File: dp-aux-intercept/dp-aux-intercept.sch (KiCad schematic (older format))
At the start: 24 parts, among them J1 CONN_02X03, J2 CONN_02X03

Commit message: Initial scatter.
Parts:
- CCAN1, CCAP1, CDAN1, CDAP1: footprint (none) -> Capacitors_SMD:C_0805_HandSoldering
- DPC1, DPD1: footprint (none) -> display_port:display_port
- J1, J2: footprint (none) -> Pin_Headers:Pin_Header_Straight_2x03
- PAUX1, PCONF1: footprint (none) -> Pin_Headers:Pin_Header_Straight_2x06
- RCAN1, RCAN2, RCAP1, RCAP2, RCCFG1, RCCFG2, RCHPD1, RDAN1, RDAN2, RDAP1, RDAP2, RDCFG1, RDCFG2, RDHPD1: footprint (none) -> Resistors_SMD:R_0603_HandSoldering
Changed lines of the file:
@@
 F 0 "DPC1" H 1510 3310 60  0000 C CNN
 F 1 "DISPLAY_PORT" V 2260 2210 60  0000 C CNN
-F 2 "" H 2060 2210 60  0000 C CNN
+F 2 "display_port:display_port" H 2060 2210 60  0001 C CNN
 F 3 "" H 2060 2210 60  0000 C CNN
 	1    2110 2210
@@
 F 0 "PAUX1" H 5510 4690 50  0000 C CNN
 F 1 "CONN_02X06" H 5510 3990 50  0000 C CNN
-F 2 "" H 5510 3140 60  0000 C CNN
+F 2 "Pin_Headers:Pin_Header_Straight_2x06" H 5510 3140 60  0001 C CNN
 F 3 "" H 5510 3140 60  0000 C CNN
 	1    5510 4340
@@
 F 0 "DPD1" H 8400 3310 60  0000 C CNN
 F 1 "DISPLAY_PORT" V 9150 2210 60  0000 C CNN
-F 2 "" H 8950 2210 60  0000 C CNN
+F 2 "display_port:display_port" H 8950 2210 60  0001 C CNN
 F 3 "" H 8950 2210 60  0000 C CNN
 	1    9000 2210
@@
 F 0 "PCONF1" H 5580 3110 50  0000 C CNN
 F 1 "CONN_02X06" H 5580 2410 50  0000 C CNN
-F 2 "" H 5580 1560 60  0000 C CNN
+F 2 "Pin_Headers:Pin_Header_Straight_2x06" H 5580 1560 60  0001 C CNN
 F 3 "" H 5580 1560 60  0000 C CNN
 	1    5580 2760
@@
 F 0 "RDCFG1" V 7230 2890 50  0000 C CNN
 F 1 "1M" V 7150 2890 50  0000 C CNN
-F 2 "" V 7080 2890 30  0000 C CNN
+F 2 "Resistors_SMD:R_0603_HandSoldering" V 7080 2890 30  0001 C CNN
 F 3 "" H 7150 2890 30  0000 C CNN
 	1    7150 2890
@@
 F 0 "RDCFG2" V 7230 3060 50  0000 C CNN
 F 1 "5M" V 7150 3060 50  0000 C CNN
-F 2 "" V 7080 3060 30  0000 C CNN
+F 2 "Resistors_SMD:R_0603_HandSoldering" V 7080 3060 30  0001 C CNN
 F 3 "" H 7150 3060 30  0000 C CNN
 	1    7150 3060
@@
 F 0 "RDHPD1" V 7230 3230 50  0000 C CNN
 F 1 "100K" V 7150 3230 50  0000 C CNN
-F 2 "" V 7080 3230 30  0000 C CNN
+F 2 "Resistors_SMD:R_0603_HandSoldering" V 7080 3230 30  0001 C CNN
 F 3 "" H 7150 3230 30  0000 C CNN
 	1    7150 3230
@@
 F 0 "J2" H 6590 3190 50  0000 C CNN
 F 1 "CONN_02X03" H 6590 2790 50  0000 C CNN
-F 2 "" H 6590 1790 60  0000 C CNN
+F 2 "Pin_Headers:Pin_Header_Straight_2x03" H 6590 1790 60  0001 C CNN
 F 3 "" H 6590 1790 60  0000 C CNN
 	1    6590 2990
@@
 F 0 "RCCFG1" V 4040 2890 50  0000 C CNN
 F 1 "1M" V 3960 2890 50  0000 C CNN
-F 2 "" V 3890 2890 30  0000 C CNN
+F 2 "Resistors_SMD:R_0603_HandSoldering" V 3890 2890 30  0001 C CNN
 F 3 "" H 3960 2890 30  0000 C CNN
 	1    3960 2890
@@
 F 0 "RCCFG2" V 4040 3060 50  0000 C CNN
 F 1 "5M" V 3960 3060 50  0000 C CNN
-F 2 "" V 3890 3060 30  0000 C CNN
+F 2 "Resistors_SMD:R_0603_HandSoldering" V 3890 3060 30  0001 C CNN
 F 3 "" H 3960 3060 30  0000 C CNN
 	1    3960 3060
@@
 F 0 "RCHPD1" V 4040 3230 50  0000 C CNN
 F 1 "100K" V 3960 3230 50  0000 C CNN
-F 2 "" V 3890 3230 30  0000 C CNN
+F 2 "Resistors_SMD:R_0603_HandSoldering" V 3890 3230 30  0001 C CNN
 F 3 "" H 3960 3230 30  0000 C CNN
 	1    3960 3230
@@
 F 0 "J1" H 4520 3190 50  0000 C CNN
 F 1 "CONN_02X03" H 4520 2790 50  0000 C CNN
-F 2 "" H 4520 1790 60  0000 C CNN
+F 2 "Pin_Headers:Pin_Header_Straight_2x03" H 4520 1790 60  0001 C CNN
 F 3 "" H 4520 1790 60  0000 C CNN
 	1    4520 2990
@@
 F 0 "RCAP1" V 3990 4270 50  0000 C CNN
 F 1 "100K" V 3910 4270 50  0000 C CNN
-F 2 "" V 3840 4270 30  0000 C CNN
+F 2 "Resistors_SMD:R_0603_HandSoldering" V 3840 4270 30  0001 C CNN
 F 3 "" H 3910 4270 30  0000 C CNN
 	1    3910 4270
@@
 F 0 "RCAN1" V 3990 4640 50  0000 C CNN
 F 1 "100K" V 3910 4640 50  0000 C CNN
-F 2 "" V 3840 4640 30  0000 C CNN
+F 2 "Resistors_SMD:R_0603_HandSoldering" V 3840 4640 30  0001 C CNN
 F 3 "" H 3910 4640 30  0000 C CNN
 	1    3910 4640
@@
 F 0 "RCAP2" V 4440 4270 50  0000 C CNN
 F 1 "50" V 4360 4270 50  0000 C CNN
-F 2 "" V 4290 4270 30  0000 C CNN
+F 2 "Resistors_SMD:R_0603_HandSoldering" V 4290 4270 30  0001 C CNN
 F 3 "" H 4360 4270 30  0000 C CNN
 	1    4360 4270
@@
 F 0 "RCAN2" V 4440 4640 50  0000 C CNN
 F 1 "50" V 4360 4640 50  0000 C CNN
-F 2 "" V 4290 4640 30  0000 C CNN
+F 2 "Resistors_SMD:R_0603_HandSoldering" V 4290 4640 30  0001 C CNN
 F 3 "" H 4360 4640 30  0000 C CNN
 	1    4360 4640
@@
 F 0 "CCAP1" H 4165 4190 50  0000 L CNN
 F 1 "C" H 4165 3990 50  0000 L CNN
-F 2 "" H 4178 3940 30  0000 C CNN
+F 2 "Capacitors_SMD:C_0805_HandSoldering" H 4178 3940 30  0001 C CNN
 F 3 "" H 4140 4090 60  0000 C CNN
 	1    4140 4090
@@
 F 0 "CCAN1" H 4165 4930 50  0000 L CNN
 F 1 "C" H 4165 4730 50  0000 L CNN
-F 2 "" H 4178 4680 30  0000 C CNN
+F 2 "Capacitors_SMD:C_0805_HandSoldering" H 4178 4680 30  0001 C CNN
 F 3 "" H 4140 4830 60  0000 C CNN
 	1    4140 4830
@@
 F 0 "RDAP2" V 6790 4270 50  0000 C CNN
 F 1 "50" V 6710 4270 50  0000 C CNN
-F 2 "" V 6640 4270 30  0000 C CNN
+F 2 "Resistors_SMD:R_0603_HandSoldering" V 6640 4270 30  0001 C CNN
 F 3 "" H 6710 4270 30  0000 C CNN
 	1    6710 4270
@@
 F 0 "RDAN2" V 6790 4640 50  0000 C CNN
 F 1 "50" V 6710 4640 50  0000 C CNN
-F 2 "" V 6640 4640 30  0000 C CNN
+F 2 "Resistors_SMD:R_0603_HandSoldering" V 6640 4640 30  0001 C CNN
 F 3 "" H 6710 4640 30  0000 C CNN
 	1    6710 4640
@@
 F 0 "RDAP1" V 7240 4270 50  0000 C CNN
 F 1 "10K" V 7160 4270 50  0000 C CNN
-F 2 "" V 7090 4270 30  0000 C CNN
+F 2 "Resistors_SMD:R_0603_HandSoldering" V 7090 4270 30  0001 C CNN
 F 3 "" H 7160 4270 30  0000 C CNN
 	1    7160 4270
@@
 F 0 "RDAN1" V 7240 4640 50  0000 C CNN
 F 1 "10K" V 7160 4640 50  0000 C CNN
-F 2 "" V 7090 4640 30  0000 C CNN
+F 2 "Resistors_SMD:R_0603_HandSoldering" V 7090 4640 30  0001 C CNN
 F 3 "" H 7160 4640 30  0000 C CNN
 	1    7160 4640
@@
 F 0 "CDAP1" H 6965 4190 50  0000 L CNN
 F 1 "C" H 6965 3990 50  0000 L CNN
-F 2 "" H 6978 3940 30  0000 C CNN
+F 2 "Capacitors_SMD:C_0805_HandSoldering" H 6978 3940 30  0001 C CNN
 F 3 "" H 6940 4090 60  0000 C CNN
 	1    6940 4090
@@
 F 0 "CDAN1" H 6965 4930 50  0000 L CNN
 F 1 "C" H 6965 4730 50  0000 L CNN
-F 2 "" H 6978 4680 30  0000 C CNN
+F 2 "Capacitors_SMD:C_0805_HandSoldering" H 6978 4680 30  0001 C CNN
 F 3 "" H 6940 4830 60  0000 C CNN
 	1    6940 4830

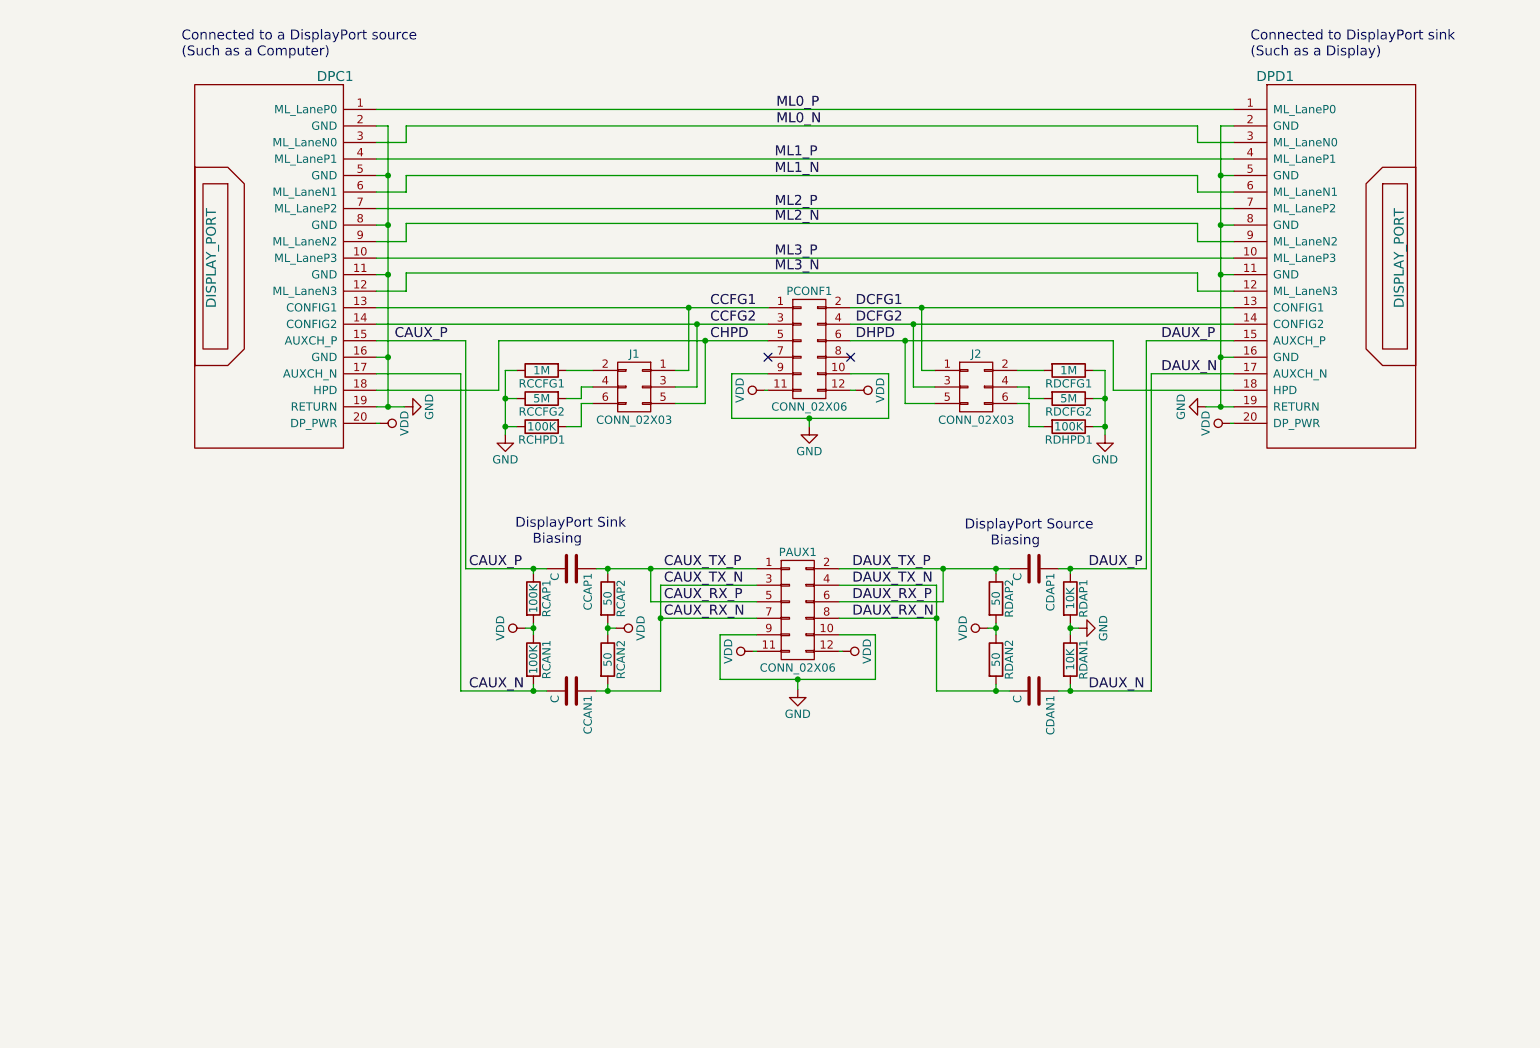
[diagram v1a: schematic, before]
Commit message: Adding schematic description.
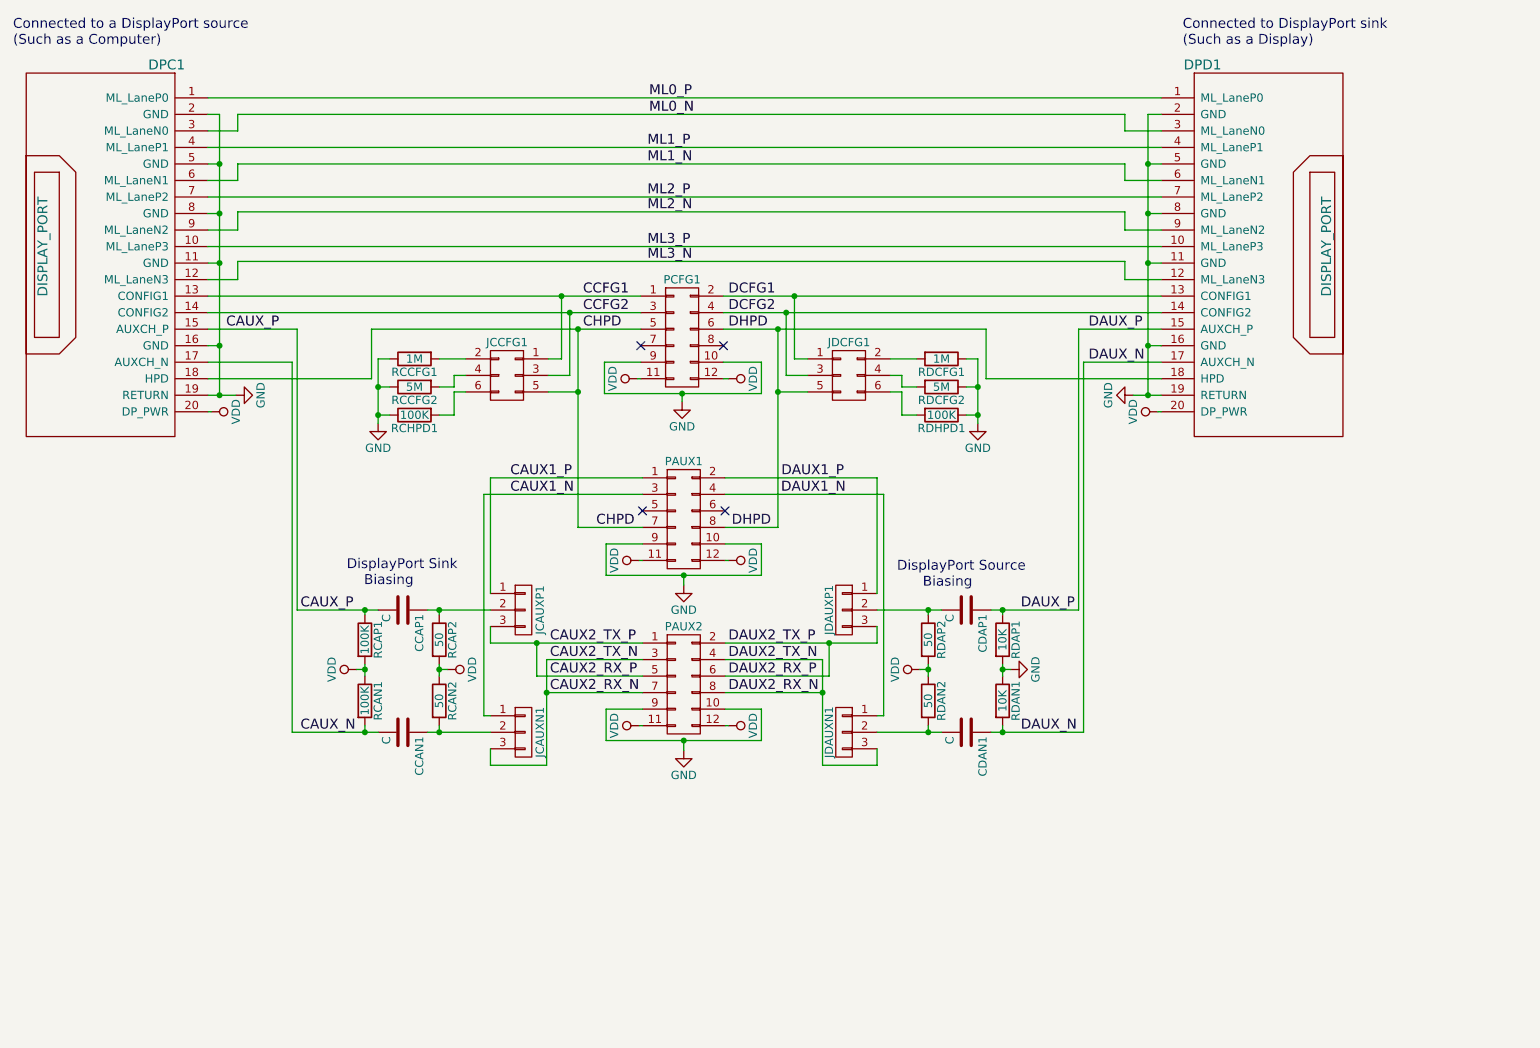
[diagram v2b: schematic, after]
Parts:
- added JCAUXN1, JCAUXP1, JDAUXN1, JDAUXP1: CONN_01X03, symbol CONN_01X03
- added PAUX1: CONN_02X06, Pin_Headers:Pin_Header_Straight_2x06, symbol CONN_02X06
- renumbered J1 to JCCFG1, J2 to JDCFG1, PAUX1 to PAUX2, PCONF1 to PCFG1
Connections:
- net CHPD: now also PAUX1.7 (P7)
- net DHPD: now also PAUX1.8 (P8)
- net GND: now also PAUX1.10 (P10), PAUX1.9 (P9)
- net VDD: now also PAUX1.11 (P11), PAUX1.12 (P12)
- net CAUX_RX_N: no longer names the net of CCAN1.1, RCAN2.2
- net CAUX_RX_N: now also JCAUXN1.2 (P2); no longer PAUX2.3 (P3), PAUX2.7 (P7)
- net CAUX_RX_P: no longer names the net of CCAP1.1, RCAP2.1
- net CAUX_RX_P: now also JCAUXP1.2 (P2); no longer PAUX2.1 (P1), PAUX2.5 (P5)
- net DAUX_RX_N: no longer names the net of CDAN1.2, RDAN2.2
- net DAUX_RX_N: now also JDAUXN1.2 (P2); no longer PAUX2.4 (P4), PAUX2.8 (P8)
- net DAUX_RX_P: no longer names the net of CDAP1.2, RDAP2.1
- net DAUX_RX_P: now also JDAUXP1.2 (P2); no longer PAUX2.2 (P2), PAUX2.6 (P6)
- new net CAUX1_N: JCAUXN1.1 (P1), PAUX1.3 (P3)
- new net CAUX1_P: JCAUXP1.1 (P1), PAUX1.1 (P1)
- new net CAUX2_RX_N: JCAUXN1.3 (P3), PAUX2.3 (P3), PAUX2.7 (P7)
- new net CAUX2_RX_P: JCAUXP1.3 (P3), PAUX2.1 (P1), PAUX2.5 (P5)
- new net DAUX1_N: JDAUXN1.1 (P1), PAUX1.4 (P4)
- new net DAUX1_P: JDAUXP1.1 (P1), PAUX1.2 (P2)
- new net DAUX2_RX_N: JDAUXN1.3 (P3), PAUX2.4 (P4), PAUX2.8 (P8)
- new net DAUX2_RX_P: JDAUXP1.3 (P3), PAUX2.2 (P2), PAUX2.6 (P6)
- no-connect marks 2 -> 4
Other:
- moved on the sheet: CCAN1, CCAP1, CDAN1, CDAP1, DPC1, DPD1, JCCFG1, JDCFG1, PAUX2, PCFG1, RCAN1, RCAN2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

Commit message: Changing to using the through-hole DisplayPort connectors.
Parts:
- DPC1, DPD1: footprint display_port:display_port -> 2040204-1:2040210-1
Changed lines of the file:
@@
 F 0 "DPC1" H 490 3240 60  0000 C CNN
 F 1 "DISPLAY_PORT" V 1240 2140 60  0000 C CNN
-F 2 "display_port:display_port" H 1040 2140 60  0001 C CNN
+F 2 "2040204-1:2040210-1" H 1040 2140 60  0001 C CNN
 F 3 "" H 1040 2140 60  0000 C CNN
 	1    1090 2140
@@
 F 0 "DPD1" H 7960 3240 60  0000 C CNN
 F 1 "DISPLAY_PORT" V 8710 2140 60  0000 C CNN
-F 2 "display_port:display_port" H 8510 2140 60  0001 C CNN
+F 2 "2040204-1:2040210-1" H 8510 2140 60  0001 C CNN
 F 3 "" H 8510 2140 60  0000 C CNN
 	1    8560 2140
@@
 	1940 1340 2010 1340
 Wire Wire Line
-	2010 1340 2010 1640
-Wire Wire Line
-	2010 1640 2010 1940
-Wire Wire Line
-	2010 1940 2010 2240
-Wire Wire Line
-	2010 2240 2010 2740
-Wire Wire Line
-	2010 2740 2010 3040
-Wire Wire Line
-	1940 3040 2010 3040
-Wire Wire Line
-	2010 3040 2110 3040
+	2010 1340 2010 3040
+Wire Wire Line
+	1940 3040 2110 3040
 Wire Wire Line
 	1940 1640 2010 1640
@@
 	7710 1340 7630 1340
 Wire Wire Line
-	7630 1340 7630 1640
-Wire Wire Line
-	7630 1640 7630 1940
-Wire Wire Line
-	7630 1940 7630 2240
-Wire Wire Line
-	7630 2240 7630 2740
-Wire Wire Line
-	7630 2740 7630 3040
-Wire Wire Line
-	7540 3040 7630 3040
-Wire Wire Line
-	7630 3040 7710 3040
+	7630 1340 7630 3040
+Wire Wire Line
+	7540 3040 7710 3040
 Wire Wire Line
 	7710 1640 7630 1640
@@
 	5070 4940 5290 4940
 Wire Wire Line
-	5290 4940 5290 5130
-Wire Wire Line
-	5290 5130 4820 5130
-Wire Wire Line
-	4820 5130 4350 5130
+	5290 5130 5290 4940
+Wire Wire Line
+	4350 5130 5290 5130
 Wire Wire Line
 	1940 2640 2480 2640
@@
 	5060 2840 5290 2840
 Wire Wire Line
-	5070 4540 5700 4540
-Wire Wire Line
-	5700 4540 5990 4540
-Wire Wire Line
-	5990 4340 6300 4340
-Wire Wire Line
-	6300 4340 6380 4340
+	5070 4540 5990 4540
+Wire Wire Line
+	5990 4340 6380 4340
 Wire Wire Line
 	5070 4640 5660 4640
 Wire Wire Line
-	3270 4340 3340 4340
-Wire Wire Line
-	3340 4340 3650 4340
-Wire Wire Line
-	3650 4540 3930 4540
-Wire Wire Line
-	3930 4540 4570 4540
+	3270 4340 3650 4340
+Wire Wire Line
+	3650 4540 4570 4540
 Wire Wire Line
 	3990 4640 4570 4640
 Wire Wire Line
-	1940 2440 4080 2440
-Wire Wire Line
-	4080 2440 4560 2440
-Wire Wire Line
-	1940 2540 4130 2540
-Wire Wire Line
-	4130 2540 4560 2540
-Wire Wire Line
-	5060 2440 5490 2440
-Wire Wire Line
-	5490 2440 7710 2440
-Wire Wire Line
-	5060 2540 5440 2540
-Wire Wire Line
-	5440 2540 7710 2540
+	1940 2440 4560 2440
+Wire Wire Line
+	1940 2540 4560 2540
+Wire Wire Line
+	5060 2440 7710 2440
+Wire Wire Line
+	5060 2540 7710 2540
 Wire Wire Line
 	5070 4740 5700 4740
@@
 	6600 3160 6530 3160
 Wire Wire Line
-	6600 2820 6600 2990
-Wire Wire Line
-	6600 2990 6600 3160
-Wire Wire Line
-	6600 3160 6600 3210
+	6600 2820 6600 3210
 Wire Wire Line
 	6530 2990 6600 2990
@@
 	6140 3160 6230 3160
 Wire Wire Line
-	5060 2640 5390 2640
-Wire Wire Line
-	5390 2640 6650 2640
-Wire Wire Line
-	5390 2640 5390 3020
-Wire Wire Line
-	5390 3020 5390 3840
+	5060 2640 6650 2640
+Wire Wire Line
+	5390 2640 5390 3840
 Wire Wire Line
 	5390 3020 5570 3020
@@
 	2970 3160 3040 3160
 Wire Wire Line
-	2970 2820 2970 2990
-Wire Wire Line
-	2970 2990 2970 3160
-Wire Wire Line
-	2970 3160 2970 3210
+	2970 2820 2970 3210
 Wire Wire Line
 	3040 2990 2970 2990
@@
 	3430 3160 3340 3160
 Wire Wire Line
-	4180 2640 4180 3020
-Wire Wire Line
-	4180 3020 4180 3840
+	4180 2640 4180 3840
 Wire Wire Line
 	4180 3020 4000 3020
@@
 	2930 2940 2930 2640
 Wire Wire Line
-	2930 2640 4180 2640
-Wire Wire Line
-	4180 2640 4560 2640
-Wire Wire Line
-	5290 2840 5290 3030
-Wire Wire Line
-	5290 3030 4810 3030
-Wire Wire Line
-	4810 3030 4340 3030
+	2930 2640 4560 2640
+Wire Wire Line
+	5290 3030 5290 2840
+Wire Wire Line
+	4340 3030 5290 3030
 Wire Wire Line
 	4340 3030 4340 2840
@@
 	7240 5080 7240 2840
 Wire Wire Line
-	3340 4670 3340 4700
-Wire Wire Line
-	3340 4700 3340 4740
+	3340 4670 3340 4740
 Wire Wire Line
 	3340 4700 3390 4700
 Connection ~ 3340 4700
 Wire Wire Line
-	2890 4670 2890 4700
-Wire Wire Line
-	2890 4700 2890 4740
+	2890 4670 2890 4740
 Wire Wire Line
 	2890 4700 2840 4700
 Connection ~ 2890 4700
 Wire Wire Line
-	2480 4340 2890 4340
-Wire Wire Line
-	2890 4340 2970 4340
+	2480 4340 2970 4340
 Wire Wire Line
 	2890 4370 2890 4340
@@
 Connection ~ 3340 4340
 Wire Wire Line
-	3270 5080 3340 5080
-Wire Wire Line
-	3340 5080 3650 5080
+	3270 5080 3650 5080
 Wire Wire Line
 	3340 5080 3340 5040
 Connection ~ 3340 5080
 Wire Wire Line
-	2450 5080 2890 5080
-Wire Wire Line
-	2890 5080 2970 5080
+	2450 5080 2970 5080
 Wire Wire Line
 	2890 5080 2890 5040
@@
 $EndComp
 Wire Wire Line
-	6750 4670 6750 4700
-Wire Wire Line
-	6750 4700 6750 4740
+	6750 4670 6750 4740
 Wire Wire Line
 	6750 4700 6800 4700
 Connection ~ 6750 4700
 Wire Wire Line
-	6300 4670 6300 4700
-Wire Wire Line
-	6300 4700 6300 4740
+	6300 4670 6300 4740
 Wire Wire Line
 	6300 4700 6250 4700
@@
 Connection ~ 6300 4340
 Wire Wire Line
-	6680 4340 6750 4340
-Wire Wire Line
-	6750 4340 7210 4340
+	6680 4340 7210 4340
 Wire Wire Line
 	6750 4370 6750 4340
 Connection ~ 6750 4340
 Wire Wire Line
-	6680 5080 6750 5080
-Wire Wire Line
-	6750 5080 7240 5080
+	6680 5080 7240 5080
 Wire Wire Line
 	6750 5080 6750 5040
 Connection ~ 6750 5080
 Wire Wire Line
-	5990 5080 6300 5080
-Wire Wire Line
-	6300 5080 6380 5080
+	5990 5080 6380 5080
 Wire Wire Line
 	6300 5080 6300 5040
@@
 Connection ~ 3930 4540
 Wire Wire Line
-	3990 4640 3990 4840
-Wire Wire Line
-	3990 4840 3990 5280
+	3990 4640 3990 5280
 Connection ~ 3990 4840
 Wire Wire Line
@@
 	4550 5040 4570 5040
 Wire Wire Line
-	5660 4640 5660 4840
-Wire Wire Line
-	5660 4840 5660 5280
+	5660 4640 5660 5280
 Connection ~ 5660 4840
 Wire Wire Line
@@
 	5990 5280 5660 5280
 $Comp
-L VDD #PWR?
+L VDD #PWR017
 U 1 1 557C8F8E
 P 4550 4040
-F 0 "#PWR?" H 4550 3890 50  0001 C CNN
+F 0 "#PWR017" H 4550 3890 50  0001 C CNN
 F 1 "VDD" H 4550 4190 50  0000 C CNN
 F 2 "" H 4550 4040 60  0000 C CNN
@@
 $EndComp
 $Comp
-L VDD #PWR?
+L VDD #PWR018
 U 1 1 557C8FD3
 P 5090 4040
-F 0 "#PWR?" H 5090 3890 50  0001 C CNN
+F 0 "#PWR018" H 5090 3890 50  0001 C CNN
 F 1 "VDD" H 5090 4190 50  0000 C CNN
 F 2 "" H 5090 4040 60  0000 C CNN
@@
 	5070 4040 5090 4040
 $Comp
-L GND #PWR?
+L GND #PWR019
 U 1 1 557C93CE
 P 4820 4190
-F 0 "#PWR?" H 4820 3940 50  0001 C CNN
+F 0 "#PWR019" H 4820 3940 50  0001 C CNN
 F 1 "GND" H 4820 4040 50  0000 C CNN
 F 2 "" H 4820 4190 60  0000 C CNN
@@
 	5290 4130 5290 3940
 Wire Wire Line
-	4350 4130 4820 4130
-Wire Wire Line
-	4820 4130 5290 4130
+	4350 4130 5290 4130
 Wire Wire Line
 	4820 4130 4820 4190

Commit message: Changing the PAUX1 and PAUX2 to be right angle connectors.
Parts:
- PAUX1, PAUX2: footprint Pin_Headers:Pin_Header_Straight_2x06 -> Pin_Headers:Pin_Header_Angled_2x06
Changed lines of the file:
@@
 F 0 "PAUX2" H 4820 5140 50  0000 C CNN
 F 1 "CONN_02X06" H 4820 4440 50  0001 C CNN
-F 2 "Pin_Headers:Pin_Header_Straight_2x06" H 4820 3590 60  0001 C CNN
+F 2 "Pin_Headers:Pin_Header_Angled_2x06" H 4820 3590 60  0001 C CNN
 F 3 "" H 4820 3590 60  0000 C CNN
 	1    4820 4790
@@
 F 0 "PAUX1" H 4820 4140 50  0000 C CNN
 F 1 "CONN_02X06" H 4820 3440 50  0001 C CNN
-F 2 "Pin_Headers:Pin_Header_Straight_2x06" H 4820 2590 60  0001 C CNN
+F 2 "Pin_Headers:Pin_Header_Angled_2x06" H 4820 2590 60  0001 C CNN
 F 3 "" H 4820 2590 60  0000 C CNN
 	1    4820 3790
@@
 F 0 "JCAUXP1" V 3950 4340 50  0000 C CNN
 F 1 "CONN_01X03" V 3950 4340 50  0001 C CNN
-F 2 "" H 3850 4340 60  0000 C CNN
+F 2 "" H 3850 4340 60  0001 C CNN
 F 3 "" H 3850 4340 60  0000 C CNN
 	1    3850 4340
@@
 F 0 "JCAUXN1" V 3950 5080 50  0000 C CNN
 F 1 "CONN_01X03" V 3950 5080 50  0001 C CNN
-F 2 "" H 3850 5080 60  0000 C CNN
+F 2 "" H 3850 5080 60  0001 C CNN
 F 3 "" H 3850 5080 60  0000 C CNN
 	1    3850 5080
@@
 F 0 "JDAUXP1" V 5880 4340 50  0000 C CNN
 F 1 "CONN_01X03" V 5890 4340 50  0001 C CNN
-F 2 "" H 5790 4340 60  0000 C CNN
+F 2 "" H 5790 4340 60  0001 C CNN
 F 3 "" H 5790 4340 60  0000 C CNN
 	1    5790 4340
@@
 F 0 "JDAUXN1" V 5880 5080 50  0000 C CNN
 F 1 "CONN_01X03" V 5890 5080 50  0001 C CNN
-F 2 "" H 5790 5080 60  0000 C CNN
+F 2 "" H 5790 5080 60  0001 C CNN
 F 3 "" H 5790 5080 60  0000 C CNN
 	1    5790 5080
